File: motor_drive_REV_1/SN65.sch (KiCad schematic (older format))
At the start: 15 parts, among them U6 SN65LBC176QDRQ1

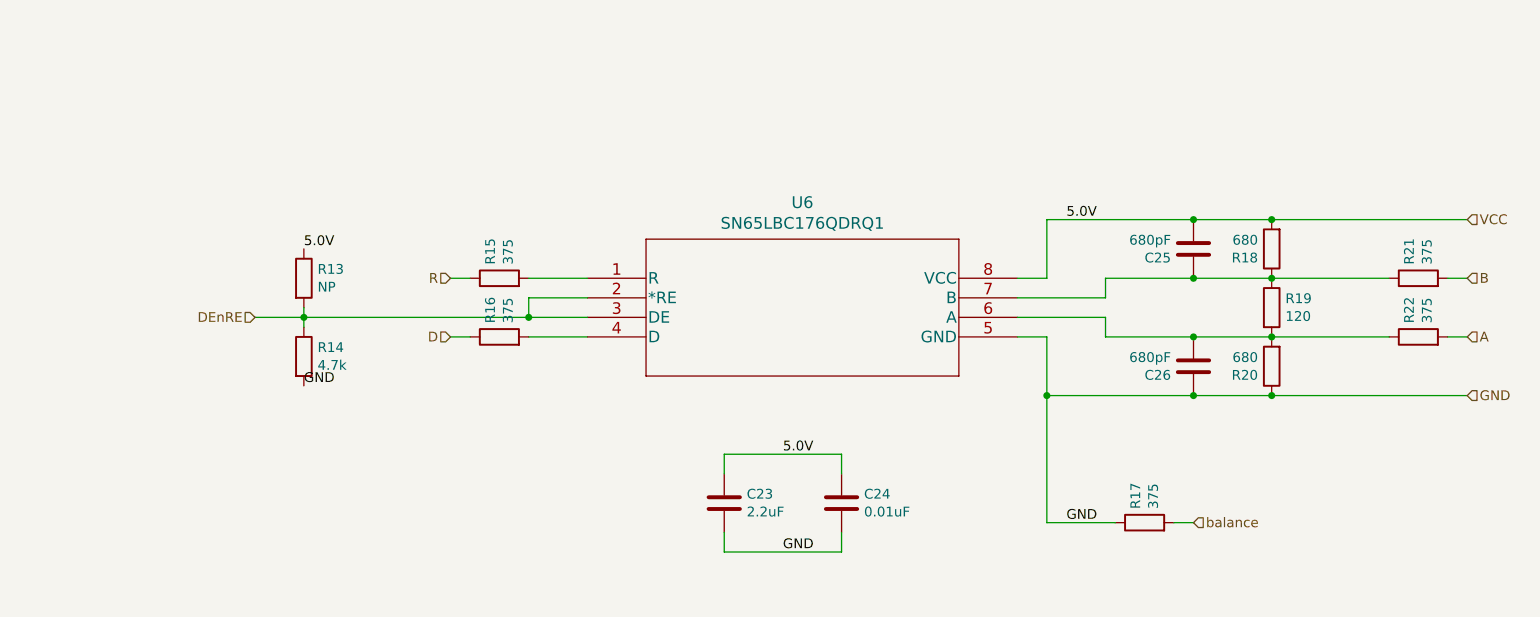
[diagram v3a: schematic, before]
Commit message: gate drive rework and schematic re-organization
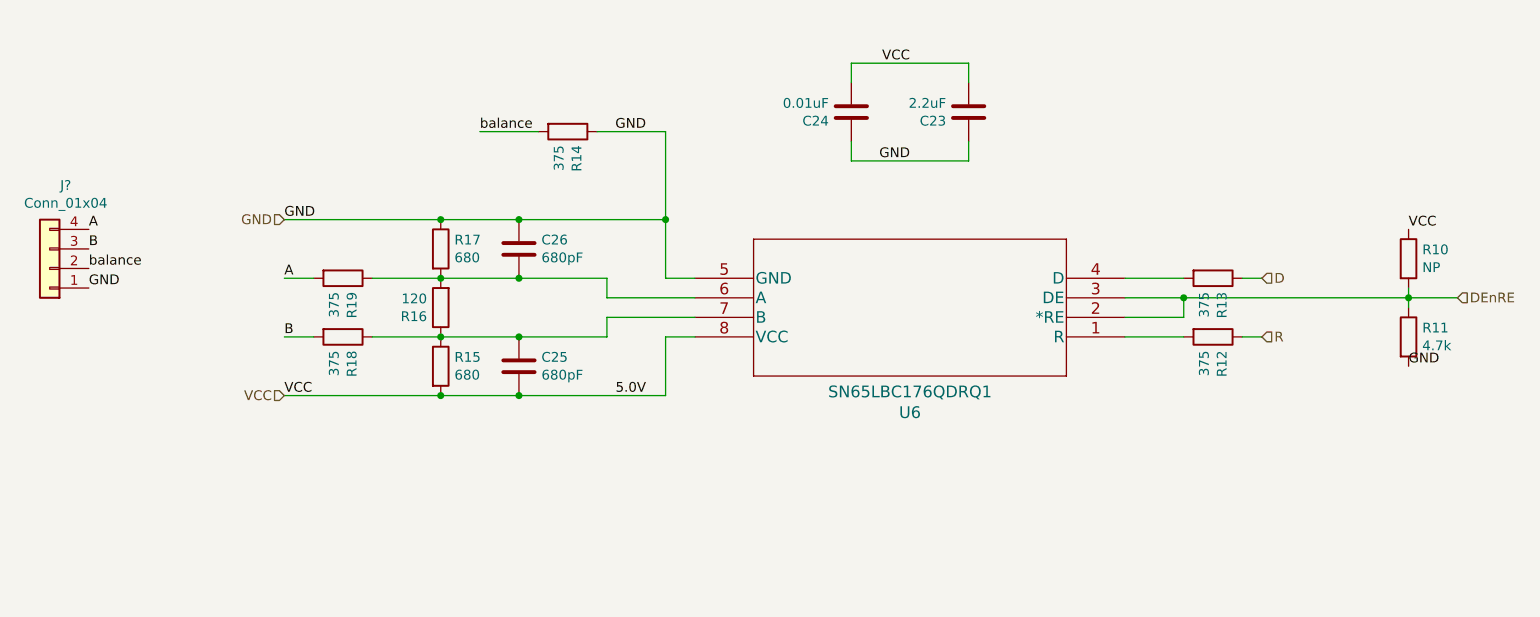
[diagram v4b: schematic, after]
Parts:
- added J?: Conn_01x04, motor_drive_footprints:4pos_254, symbol Connector_Generic:Conn_01x04
- renumbered R13 to R10, R14 to R11, R15 to R12, R16 to R13, R17 to R14, R18 to R15, R19 to R16, R20 to R17, R21 to R18, R22 to R19
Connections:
- net A: now also J?.4 (Pin_4)
- net B: now also J?.3 (Pin_3)
- net GND: now also C23.1, C24.1, J?.1 (Pin_1); no longer C23.2, C24.2
- net VCC: now also C23.2, C24.2; no longer C23.1, C24.1
- net balance: now also J?.2 (Pin_2)
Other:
- moved on the sheet: C23, C24, C25, C26, R10, R11, R12, R13, R14, R15, R16, R17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

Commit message: second try at layout
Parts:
- gave numbers to parts that had none: 1
- renumbered C26 to C3, C25 to C4, C24 to C5, C23 to C6, R19 to R1, R11 to R10, R18 to R2, R17 to R3, R16 to R4, R15 to R5, R14 to R6, R13 to R7, R12 to R8, R10 to R9, U6 to U2
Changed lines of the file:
@@
 	7850 3700 7850 3600
 $Comp
-L motor_drive:R R10
+L motor_drive:R R9
 U 1 1 5E39658B
 P 9000 3400
-F 0 "R10" H 9070 3446 50  0000 L CNN
+F 0 "R9" H 9070 3446 50  0000 L CNN
 F 1 "NP" H 9070 3355 50  0000 L CNN
 F 2 "motor_drive_footprints:C_0603_1608Metric" V 8930 3400 50  0001 C CNN
@@
 	9000 3600 9000 3550
 $Comp
-L motor_drive:C C23
+L motor_drive:C C6
 U 1 1 5E39B417
 P 6750 2650
-F 0 "C23" H 6865 2696 50  0000 L CNN
+F 0 "C6" H 6865 2696 50  0000 L CNN
 F 1 "2.2uF" H 6865 2605 50  0000 L CNN
 F 2 "motor_drive_footprints:C_0603_1608Metric" H 6788 2500 50  0001 C CNN
@@
 $EndComp
 $Comp
-L motor_drive:SN65LBC176QDRQ1 U6
+L motor_drive:SN65LBC176QDRQ1 U2
 U 1 1 5E3956B5
 P 7550 3800
-F 0 "U6" H 8650 4187 60  0000 C CNN
+F 0 "U2" H 8650 4187 60  0000 C CNN
 F 1 "SN65LBC176QDRQ1" H 8650 4081 60  0000 C CNN
 F 2 "motor_drive_footprints:SN65LBC176QDRQ1" H 8650 4040 60  0001 C CNN
@@
 VCC
 $Comp
-L motor_drive:R R11
+L motor_drive:R R10
 U 1 1 5E39AB4E
 P 9000 3800
-F 0 "R11" H 9070 3846 50  0000 L CNN
+F 0 "R10" H 9070 3846 50  0000 L CNN
 F 1 "4.7k" H 9070 3755 50  0000 L CNN
 F 2 "motor_drive_footprints:C_0603_1608Metric" V 8930 3800 50  0001 C CNN
@@
 GND
 $Comp
-L motor_drive:R R12
+L motor_drive:R R8
 U 1 1 5E3A24BE
 P 8000 3800
-F 0 "R12" H 8070 3846 50  0000 L CNN
+F 0 "R8" H 8070 3846 50  0000 L CNN
 F 1 "375" H 8070 3755 50  0000 L CNN
 F 2 "motor_drive_footprints:C_0603_1608Metric" V 7930 3800 50  0001 C CNN
@@
 $EndComp
 $Comp
-L motor_drive:R R13
+L motor_drive:R R7
 U 1 1 5E3A2A5B
 P 8000 3500
-F 0 "R13" H 8070 3546 50  0000 L CNN
+F 0 "R7" H 8070 3546 50  0000 L CNN
 F 1 "375" H 8070 3455 50  0000 L CNN
 F 2 "motor_drive_footprints:C_0603_1608Metric" V 7930 3500 50  0001 C CNN
@@
 	7850 3500 7550 3500
 $Comp
-L motor_drive:R R14
+L motor_drive:R R6
 U 1 1 5E33ED83
 P 4700 2750
-F 0 "R14" H 4770 2796 50  0000 L CNN
+F 0 "R6" H 4770 2796 50  0000 L CNN
 F 1 "375" H 4770 2705 50  0000 L CNN
 F 2 "motor_drive_footprints:C_0603_1608Metric" V 4630 2750 50  0001 C CNN
@@
 	4850 2750 5200 2750
 $Comp
-L motor_drive:R R16
+L motor_drive:R R4
 U 1 1 5E390D6F
 P 4050 3650
-F 0 "R16" H 4120 3696 50  0000 L CNN
+F 0 "R4" H 4120 3696 50  0000 L CNN
 F 1 "120" H 4120 3605 50  0000 L CNN
 F 2 "motor_drive_footprints:C_0603_1608Metric" V 3980 3650 50  0001 C CNN
@@
 	4900 3600 4900 3500
 $Comp
-L motor_drive:R R17
+L motor_drive:R R3
 U 1 1 5E37C57B
 P 4050 3350
-F 0 "R17" H 4120 3396 50  0000 L CNN
+F 0 "R3" H 4120 3396 50  0000 L CNN
 F 1 "680" H 4120 3305 50  0000 L CNN
 F 2 "motor_drive_footprints:C_0603_1608Metric" V 3980 3350 50  0001 C CNN
@@
 	5350 3600 4900 3600
 $Comp
-L motor_drive:R R18
+L motor_drive:R R2
 U 1 1 5E37EDA8
 P 3550 3800
-F 0 "R18" H 3620 3846 50  0000 L CNN
+F 0 "R2" H 3620 3846 50  0000 L CNN
 F 1 "375" H 3620 3755 50  0000 L CNN
 F 2 "motor_drive_footprints:C_0603_1608Metric" V 3480 3800 50  0001 C CNN
@@
 $EndComp
 $Comp
-L motor_drive:R R19
+L motor_drive:R R1
 U 1 1 5E37F275
 P 3550 3500
-F 0 "R19" H 3620 3546 50  0000 L CNN
+F 0 "R1" H 3620 3546 50  0000 L CNN
 F 1 "375" H 3620 3455 50  0000 L CNN
 F 2 "motor_drive_footprints:C_0603_1608Metric" V 3480 3500 50  0001 C CNN
@@
 $EndComp
 $Comp
-L motor_drive:C C26
+L motor_drive:C C3
 U 1 1 5E386871
 P 4450 3350
-F 0 "C26" H 4565 3396 50  0000 L CNN
+F 0 "C3" H 4565 3396 50  0000 L CNN
 F 1 "680pF" H 4565 3305 50  0000 L CNN
 F 2 "motor_drive_footprints:C_0603_1608Metric" H 4488 3200 50  0001 C CNN
@@
 	4900 3700 4900 3800
 $Comp
-L motor_drive:C C24
+L motor_drive:C C5
 U 1 1 5E3AD083
 P 6150 2650
-F 0 "C24" H 6265 2696 50  0000 L CNN
+F 0 "C5" H 6265 2696 50  0000 L CNN
 F 1 "0.01uF" H 6265 2605 50  0000 L CNN
 F 2 "motor_drive_footprints:C_0603_1608Metric" H 6188 2500 50  0001 C CNN
@@
 	4450 3500 4050 3500
 $Comp
-L motor_drive:R R15
+L motor_drive:R R5
 U 1 1 5E5DB1A4
 P 4050 3950
-F 0 "R15" H 4120 3996 50  0000 L CNN
+F 0 "R5" H 4120 3996 50  0000 L CNN
 F 1 "680" H 4120 3905 50  0000 L CNN
 F 2 "motor_drive_footprints:C_0603_1608Metric" V 3980 3950 50  0001 C CNN
@@
 $EndComp
 $Comp
-L motor_drive:C C25
+L motor_drive:C C4
 U 1 1 5E5DB1AA
 P 4450 3950
-F 0 "C25" H 4565 3996 50  0000 L CNN
+F 0 "C4" H 4565 3996 50  0000 L CNN
 F 1 "680pF" H 4565 3905 50  0000 L CNN
 F 2 "motor_drive_footprints:C_0603_1608Metric" H 4488 3800 50  0001 C CNN
@@
 GND
 $Comp
-L Connector_Generic:Conn_01x04 J?
+L Connector_Generic:Conn_01x04 J1
 U 1 1 5E9CE42C
 P 2050 3450
-F 0 "J?" H 1968 3025 50  0000 C CNN
+F 0 "J1" H 1968 3025 50  0000 C CNN
 F 1 "Conn_01x04" H 1968 3116 50  0000 C CNN
 F 2 "motor_drive_footprints:4pos_254" H 2050 3450 50  0001 C CNN
